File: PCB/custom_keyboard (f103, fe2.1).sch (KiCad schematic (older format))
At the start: 509 parts, among them J1 Conn_01x04, U1 SD00HA, U10 PRTR5V0U2X, U11 MIC2505, U12 XC6206P332MR, U13 74LVC1G34, U2 PRTR5V0U2X, U3 PRTR5V0U2X, U4 PRTR5V0U2X, U5 24LC04BT-I/SN, U6 PRTR5V0U2X, U7 PRTR5V0U2X, U8 PRTR5V0U2X, U9 MIC2505, Y1 12MHz, Y2 8MHz

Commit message: Renamed test points, fixed DRC errors
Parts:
- renumbered TP39 to 1-4, TP52 to 5-7, TP43 to BKL3, TP53 to BKL5, TP13 to BOOT0, TP23 to BOOT1, TP17 to COL0, TP18 to COL1, TP42 to COL10, TP44 to COL11, TP46 to COL12, TP48 to COL13, TP49 to COL14, TP50 to COL15, TP38 to COL16, TP41 to COL17, TP16 to COL2, TP20 to COL3, TP22 to COL4, TP24 to COL5, TP26 to COL6, TP28 to COL7, TP31 to COL8, TP34 to COL9, TP2 to D+1, TP6 to D+2, TP3 to D+3, TP7 to D+4, TP10 to D+5, TP11 to D+6, TP32 to D+7, TP1 to D-1, TP5 to D-2, TP4 to D-3, TP8 to D-4, TP9 to D-5, TP12 to D-6, TP29 to D-7, TP36 to ENCA1, TP19 to ENCB1, TP21 to ENCB2, TP45 to KD+1, TP47 to KD-1, TP33 to KSCL1, TP35 to KSDA1, TP54 to LOGO0, TP40 to ROW0, TP37 to ROW1, TP30 to ROW2, TP27 to ROW3, TP25 to ROW4, TP51 to ROW5, RESET1 to SW1, BOOT0 to SW2, TP14 to X1, TP15 to X2
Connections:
- no-connect marks 10 -> 11

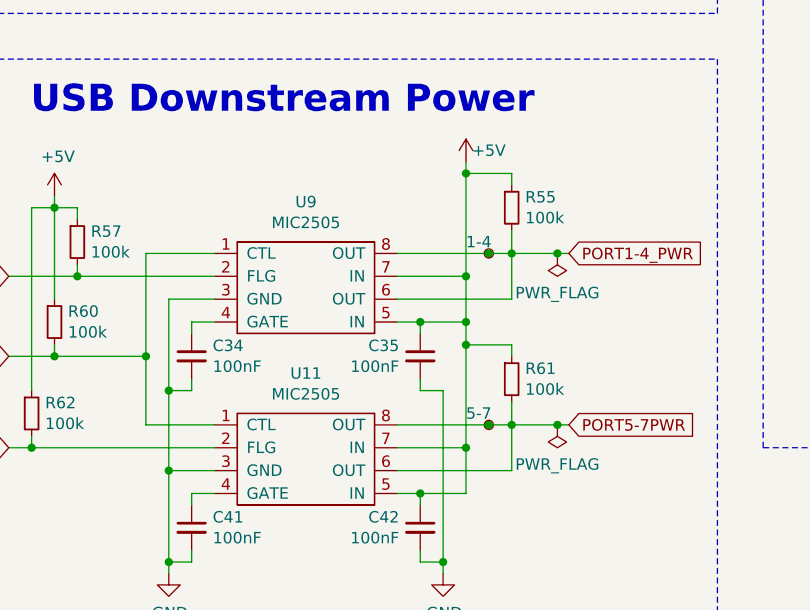
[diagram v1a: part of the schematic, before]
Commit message: Removed open load detect resistors
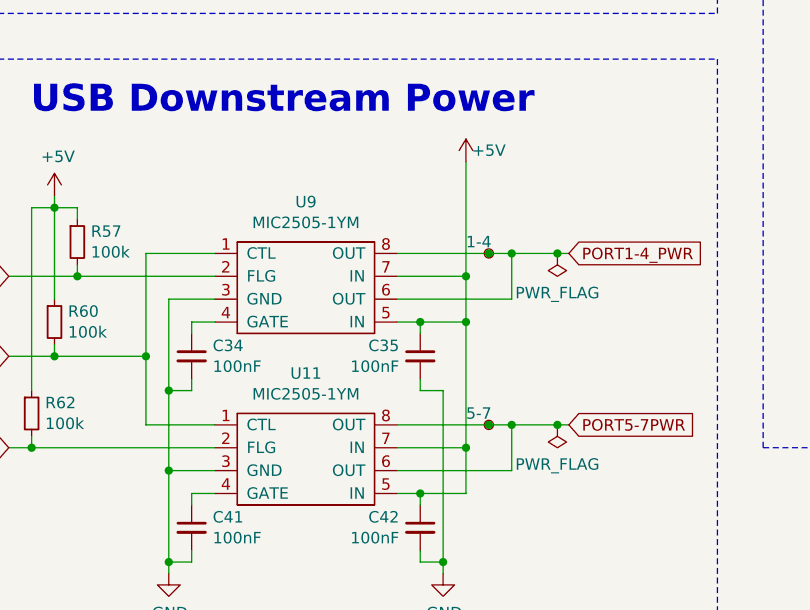
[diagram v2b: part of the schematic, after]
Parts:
- removed R55, R61: 100k, Resistor_SMD:R_0603_1608Metric, symbol Device:R_Small
- U11, U9: value MIC2505 -> MIC2505-1YM
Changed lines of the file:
@@
 P 23000 18200
 F 0 "U9" H 23000 18325 50  0000 C CNN
-F 1 "MIC2505" H 23000 18234 50  0000 C CNN
+F 1 "MIC2505-1YM" H 23000 18234 50  0000 C CNN
 F 2 "custom-footprints:MIC2505" H 23000 18200 50  0001 C CNN
 F 3 "" H 23000 18200 50  0001 C CNN
@@
 P 23000 18950
 F 0 "U11" H 23000 19075 50  0000 C CNN
-F 1 "MIC2505" H 23000 18984 50  0000 C CNN
+F 1 "MIC2505-1YM" H 23000 18984 50  0000 C CNN
 F 2 "custom-footprints:MIC2505" H 23000 18950 50  0001 C CNN
 F 3 "" H 23000 18950 50  0001 C CNN
@@
 Wire Wire Line
 	21900 18050 21900 18100
-Wire Wire Line
-	23700 18600 23700 18700
 $Comp
 L power:+5V #PWR0249
@@
 	1    0    0    -1
 $EndComp
-$Comp
-L Device:R_Small R61
-U 1 1 7460EB36
-P 23900 18850
-F 0 "R61" H 23959 18896 50  0000 L CNN
-F 1 "100k" H 23959 18805 50  0000 L CNN
-F 2 "Resistor_SMD:R_0603_1608Metric" H 23900 18850 50  0001 C CNN
-F 3 "~" H 23900 18850 50  0001 C CNN
-F 4 "C25803" H 23900 18850 50  0001 C CNN "LCSC Part"
-	1    23900 18850
-	1    0    0    -1
-$EndComp
-Wire Wire Line
-	23900 19050 23900 18950
-Wire Wire Line
-	23900 18750 23900 18700
-Wire Wire Line
-	23900 18700 23700 18700
-Connection ~ 23700 18700
-Wire Wire Line
-	23700 18700 23700 19150
 Connection ~ 23700 18400
 Wire Wire Line
@@
 	23700 18600 23700 18400
 Wire Wire Line
-	23700 17900 23700 17950
-Connection ~ 23700 17950
-Wire Wire Line
-	23700 18400 23700 17950
-Wire Wire Line
-	23900 17950 23700 17950
-Wire Wire Line
-	23900 18000 23900 17950
-Wire Wire Line
-	23900 18200 23900 18300
-$Comp
-L Device:R_Small R55
-U 1 1 7284FE9A
-P 23900 18100
-F 0 "R55" H 23959 18146 50  0000 L CNN
-F 1 "100k" H 23959 18055 50  0000 L CNN
-F 2 "Resistor_SMD:R_0603_1608Metric" H 23900 18100 50  0001 C CNN
-F 3 "~" H 23900 18100 50  0001 C CNN
-F 4 "C25803" H 23900 18100 50  0001 C CNN "LCSC Part"
-	1    23900 18100
-	1    0    0    -1
-$EndComp
-Wire Wire Line
 	27850 17950 27950 17950
 Text GLabel 28350 15350 2    50   Input ~ 0
@@
 Wire Wire Line
 	22350 12100 22350 12050
+Wire Wire Line
+	23700 17900 23700 18400
+Wire Wire Line
+	23700 18600 23700 19150
 $EndSCHEMATC

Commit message: Draft 1-5 with MCU swapped with F303
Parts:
- removed STM32: STM32F103C8T6, Package_QFP:LQFP-48_7x7mm_P0.5mm, symbol MCU_ST_STM32F1:STM32F103C8Tx
- added U14: STM32F303CBT6, Package_QFP:LQFP-48_7x7mm_P0.5mm, symbol MCU_ST_STM32F3:STM32F303CBTx
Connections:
- net +3V3: now also U14.1 (VBAT), U14.24 (VDD), U14.36 (VDD), U14.48 (VDD), U14.9 (VDDA)
- net BKL_DATA_IN_3V3: now also U14.31 (PA10)
- net BOOT0: now also U14.44 (BOOT0)
- net BOOT1: now also U14.20 (PB2)
- net COL0: now also U14.3 (PC14)
- net COL1: now also U14.4 (PC15)
- net COL10: now also U14.21 (PB10)
- net COL11: now also U14.22 (PB11)
- net COL12: now also U14.25 (PB12)
- net COL13: now also U14.26 (PB13)
- net COL14: now also U14.27 (PB14)
- net COL15: now also U14.28 (PB15)
- net COL16: now also U14.29 (PA8)
- net COL17: now also U14.30 (PA9)
- net COL2: now also U14.2 (PC13)
- net COL3: now also U14.10 (PA0)
- net COL4: now also U14.11 (PA1)
- net COL5: now also U14.12 (PA2)
- net COL6: now also U14.13 (PA3)
- net COL7: now also U14.14 (PA4)
- net COL8: now also U14.15 (PA5)
- net COL9: now also U14.16 (PA6)
- net ENCODER_A: now also U14.17 (PA7)
- net ENCODER_B1: now also U14.18 (PB0)
- net ENCODER_B2: now also U14.19 (PB1)
- net GND: now also U14.23 (VSS), U14.35 (VSS), U14.47 (VSS), U14.8 (VSSA)
- net KEYBOARD_D+: now also U14.33 (PA12)
- net KEYBOARD_D-: now also U14.32 (PA11)
- net KEYBOARD_RESET: now also U14.7 (NRST)
- net KEYBOARD_SCL: now also U14.42 (PB6)
- net KEYBOARD_SDA: now also U14.43 (PB7)
- net KEYBOARD_XTAL1: now also U14.5 (PF0)
- net KEYBOARD_XTAL2: now also U14.6 (PF1)
- net ROT1_ROW: now also U14.46 (PB9)
- net ROW1: now also U14.45 (PB8)
- net ROW2: now also U14.41 (PB5)
- net ROW3: now also U14.40 (PB4)
- net ROW4: now also U14.39 (PB3)
- net ROW5: now also U14.38 (PA15)
- net SWCLK: now also U14.37 (PA14)
- net SWDIO: now also U14.34 (PA13)
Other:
- moved on the sheet: BKL3, BKL5, BOOT0, BOOT1, C10, C11, C13, C18, C19, C20, C21, C22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

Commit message: Created copy with F303, restored original to F103
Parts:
- removed U14: STM32F303CBT6, Package_QFP:LQFP-48_7x7mm_P0.5mm, symbol MCU_ST_STM32F3:STM32F303CBTx
- added U14: STM32F103C8Tx, Package_QFP:LQFP-48_7x7mm_P0.5mm, symbol MCU_ST_STM32F1:STM32F103C8Tx
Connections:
- net +3V3: now also U14.1 (VBAT), U14.24 (VDD), U14.36 (VDD), U14.48 (VDD), U14.9 (VDDA)
- net BKL_DATA_IN_3V3: now also U14.31 (PA10)
- net BOOT0: now also U14.44 (BOOT0)
- net BOOT1: now also U14.20 (PB2)
- net COL0: now also U14.3 (PC14)
- net COL1: now also U14.4 (PC15)
- net COL10: now also U14.21 (PB10)
- net COL11: now also U14.22 (PB11)
- net COL12: now also U14.25 (PB12)
- net COL13: now also U14.26 (PB13)
- net COL14: now also U14.27 (PB14)
- net COL15: now also U14.28 (PB15)
- net COL16: now also U14.29 (PA8)
- net COL17: now also U14.30 (PA9)
- net COL2: now also U14.2 (PC13)
- net COL3: now also U14.10 (PA0)
- net COL4: now also U14.11 (PA1)
- net COL5: now also U14.12 (PA2)
- net COL6: now also U14.13 (PA3)
- net COL7: now also U14.14 (PA4)
- net COL8: now also U14.15 (PA5)
- net COL9: now also U14.16 (PA6)
- net ENCODER_A: now also U14.17 (PA7)
- net ENCODER_B1: now also U14.18 (PB0)
- net ENCODER_B2: now also U14.19 (PB1)
- net GND: now also U14.23 (VSS), U14.35 (VSS), U14.47 (VSS), U14.8 (VSSA)
- net KEYBOARD_D+: now also U14.33 (PA12)
- net KEYBOARD_D-: now also U14.32 (PA11)
- net KEYBOARD_RESET: now also U14.7 (NRST)
- net KEYBOARD_SCL: now also U14.42 (PB6)
- net KEYBOARD_SDA: now also U14.43 (PB7)
- net KEYBOARD_XTAL1: now also U14.5 (PD0)
- net KEYBOARD_XTAL2: now also U14.6 (PD1)
- net ROT1_ROW: now also U14.46 (PB9)
- net ROW1: now also U14.45 (PB8)
- net ROW2: now also U14.41 (PB5)
- net ROW3: now also U14.40 (PB4)
- net ROW4: now also U14.39 (PB3)
- net ROW5: now also U14.38 (PA15)
- net SWCLK: now also U14.37 (PA14)
- net SWDIO: now also U14.34 (PA13)
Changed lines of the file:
@@
 Wire Wire Line
 	21600 16950 21600 16850
-$Comp
-L MCU_ST_STM32F3:STM32F303CBTx U14
-U 1 1 7717DD5F
-P 6050 17550
-F 0 "U14" H 6000 15961 50  0000 C CNN
-F 1 "STM32F303CBT6" H 6000 15870 50  0000 C CNN
-F 2 "Package_QFP:LQFP-48_7x7mm_P0.5mm" H 5450 16150 50  0001 R CNN
-F 3 "http://www.st.com/st-web-ui/static/active/en/resource/technical/document/datasheet/DM00058181.pdf" H 6050 17550 50  0001 C CNN
-F 4 "C108516" H 6050 17550 50  0001 C CNN "LCSC Part"
-	1    6050 17550
-	1    0    0    -1
-$EndComp
 Wire Wire Line
 	6150 19050 6150 19100
@@
 Wire Wire Line
 	23550 16250 23650 16250
+$Comp
+L MCU_ST_STM32F1:STM32F103C8Tx U14
+U 1 1 803FC249
+P 6050 17550
+F 0 "U14" H 6000 15961 50  0000 C CNN
+F 1 "STM32F103C8Tx" H 6000 15870 50  0000 C CNN
+F 2 "Package_QFP:LQFP-48_7x7mm_P0.5mm" H 5450 16150 50  0001 R CNN
+F 3 "http://www.st.com/st-web-ui/static/active/en/resource/technical/document/datasheet/CD00161566.pdf" H 6050 17550 50  0001 C CNN
+F 4 "C8734" H 6050 17550 50  0001 C CNN "LCSC Part"
+	1    6050 17550
+	1    0    0    -1
+$EndComp
 $EndSCHEMATC
